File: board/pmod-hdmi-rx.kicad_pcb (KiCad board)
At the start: 2 copper layers, 42 x 43.3 mm, 59 parts, among them P1 PMOD-CONN_6X2, U31 XC9140, U32 REG710-DBV

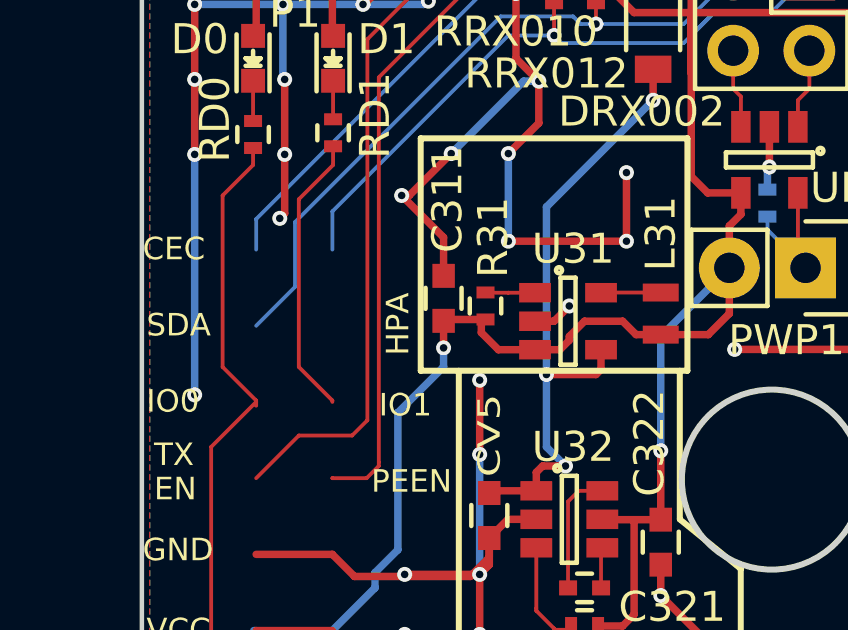
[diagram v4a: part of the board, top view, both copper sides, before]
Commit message: Update from templates + s/HPD/HOT/ + s/HPA/HOT/
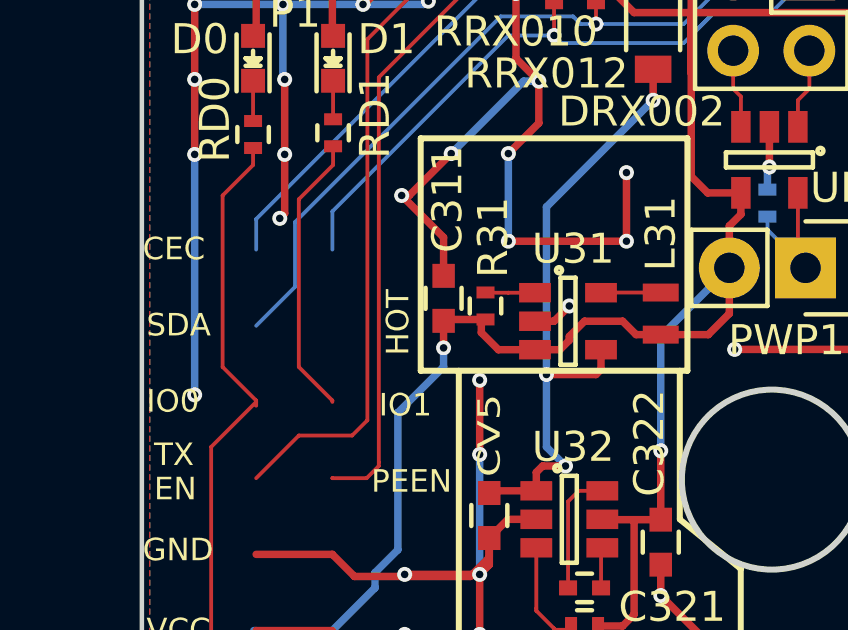
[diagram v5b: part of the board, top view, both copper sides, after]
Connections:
- net /HDMI RX/HDMIP_RX0_HPD renamed /HDMI RX/HDMIP_RX0_HOT
- P1 pad 2: /HDMI RX/HDMI_RX0_HPA -> /HDMI RX/HDMI_RX0_HOT
- QRX001 pad 1: /HDMI RX/HDMI_RX0_HPD -> /HDMI RX/HDMI_RX0_HOT
- RRX001 pad 2: /HDMI RX/HDMI_RX0_HPD -> /HDMI RX/HDMI_RX0_HOT
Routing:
- net /HDMI RX/HDMI_RX0_HPD: track 3.01 -> 0.00 mm
- net /HDMI RX/HDMI_RX0_HOT: track 0.00 -> 3.01 mm
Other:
- board text added: "HOT"
- board text removed: "HPA"
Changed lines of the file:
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@@
   (net 11 /HDMI_RX0_D2+)
   (net 12 /HDMI_RX0_D2-)
-  (net 13 "/HDMI RX/HDMIP_RX0_HPD")
+  (net 13 "/HDMI RX/HDMIP_RX0_HOT")
   (net 14 /HDMI_RX0_CEC)
   (net 15 "/HDMI RX/HDMIP_RX0_CLK+")
@@
   (net 43 /EEPROM_SCL)
   (net 44 /EEPROM_SDA)
-  (net 45 "/HDMI RX/HDMI_RX0_HPA")
+  (net 45 "/HDMI RX/HDMI_RX0_HOT")
   (net 46 /HDMI_RX0_IO1)
   (net 47 /HDMI_RX0_IO0)
@@
   (net 49 /HDMI_RX0_TXEN)
   (net 50 "Net-(PWP1-Pad1)")
-  (net 51 "/HDMI RX/HDMI_RX0_HPD")
+  (net 51 "/HDMI RX/HDMI_RX0_HOT")
   (net 52 "Net-(QRX001-Pad3)")
   (net 53 "Net-(QRX003-Pad3)")
@@
     (add_net "/HDMI RX/HDMIP_RX0_D2+")
     (add_net "/HDMI RX/HDMIP_RX0_D2-")
-    (add_net "/HDMI RX/HDMIP_RX0_HPD")
+    (add_net "/HDMI RX/HDMIP_RX0_HOT")
     (add_net "/HDMI RX/HDMIP_RX0_SCL")
     (add_net "/HDMI RX/HDMIP_RX0_SDA")
-    (add_net "/HDMI RX/HDMI_RX0_HPA")
-    (add_net "/HDMI RX/HDMI_RX0_HPD")
+    (add_net "/HDMI RX/HDMI_RX0_HOT")
+    (add_net "/HDMI RX/HDMI_RX0_HOT")
     (add_net "/HDMI RX/VCC5V0_RX0")
     (add_net "/HDMI RX/VTTI3V3")
@@
       (net 40 "Net-(FBRX004-Pad1)"))
     (pad 19 smd rect (at -4.5 -1.3 90) (size 0.3302 2.75) (layers F.Cu F.Paste F.Mask)
-      (net 13 "/HDMI RX/HDMIP_RX0_HPD"))
+      (net 13 "/HDMI RX/HDMIP_RX0_HOT"))
     (pad 0 thru_hole oval (at -7.55 0 90) (size 1.8 3.5) (drill oval 1.1 2.75) (layers *.Cu *.Mask F.SilkS))
     (pad 0 thru_hole oval (at 7.25 0 90) (size 1.8 3.5) (drill oval 1.1 2.75) (layers *.Cu *.Mask F.SilkS))
@@
     (fp_line (start -0.25 0.525) (end 0.25 0.525) (layer F.SilkS) (width 0.15))
     (pad 1 smd rect (at -0.45 0 90) (size 0.4 0.6) (layers F.Cu F.Paste F.Mask)
-      (net 13 "/HDMI RX/HDMIP_RX0_HPD"))
+      (net 13 "/HDMI RX/HDMIP_RX0_HOT"))
     (pad 2 smd rect (at 0.45 0 90) (size 0.4 0.6) (layers F.Cu F.Paste F.Mask)
       (net 38 "/HDMI RX/VCC5V0_RX0"))
@@
       (net 2 GND))
     (pad 2 smd rect (at 0.45 0 270) (size 0.4 0.6) (layers F.Cu F.Paste F.Mask)
-      (net 51 "/HDMI RX/HDMI_RX0_HPD"))
+      (net 51 "/HDMI RX/HDMI_RX0_HOT"))
     (model Resistors_SMD.3dshapes/R_0402.wrl
       (at (xyz 0 0 0))
@@
       (net 14 /HDMI_RX0_CEC))
     (pad 2 thru_hole circle (at 1.27 -3.81 270) (size 1.524 1.524) (drill 1.016) (layers *.Cu *.Mask F.SilkS)
-      (net 45 "/HDMI RX/HDMI_RX0_HPA"))
+      (net 45 "/HDMI RX/HDMI_RX0_HOT"))
     (pad 8 thru_hole circle (at -1.27 -3.81 270) (size 1.524 1.524) (drill 1.016) (layers *.Cu *.Mask F.SilkS)
       (net 28 /HDMI_RX0_SDA))
@@
     (fp_line (start 1.49982 -0.65024) (end 1.49982 0.0508) (layer F.SilkS) (width 0.15))
     (pad 1 smd rect (at -0.95 1.00076) (size 0.8001 0.8001) (layers F.Cu F.Paste F.Mask)
-      (net 51 "/HDMI RX/HDMI_RX0_HPD"))
+      (net 51 "/HDMI RX/HDMI_RX0_HOT"))
     (pad 2 smd rect (at 0.95 1.00076) (size 0.8001 0.8001) (layers F.Cu F.Paste F.Mask)
       (net 2 GND))
@@
       (net 2 GND))
     (pad 3 smd rect (at 0 -0.99822) (size 0.8001 0.8001) (layers F.Cu F.Paste F.Mask)
-      (net 13 "/HDMI RX/HDMIP_RX0_HPD"))
+      (net 13 "/HDMI RX/HDMIP_RX0_HOT"))
     (model TO_SOT_Packages_SMD.3dshapes/SOT-23.wrl
       (at (xyz 0 0 0))
@@
     (fp_line (start 1.49982 -0.65024) (end 1.49982 0.0508) (layer F.SilkS) (width 0.15))
     (pad 1 smd rect (at -0.95 1.00076) (size 0.8001 0.8001) (layers F.Cu F.Paste F.Mask)
-      (net 13 "/HDMI RX/HDMIP_RX0_HPD"))
+      (net 13 "/HDMI RX/HDMIP_RX0_HOT"))
     (pad 2 smd rect (at 0.95 1.00076) (size 0.8001 0.8001) (layers F.Cu F.Paste F.Mask)
       (net 2 GND))
@@
     (effects (font (size 1 1) (thickness 0.15)) (justify mirror))
   )
-  (gr_text HPA (at 89.662 99.314) (layer B.SilkS)
+  (gr_text HOT (at 89.662 99.314) (layer B.SilkS)
     (effects (font (size 1 1) (thickness 0.15)) (justify mirror))
   )
@@
     (effects (font (size 0.75 0.75) (thickness 0.15)) (justify left))
   )
-  (gr_text HPA (at 88.773 100.203 90) (layer F.SilkS)
+  (gr_text HOT (at 88.773 100.203 90) (layer F.SilkS)
     (effects (font (size 0.75 0.75) (thickness 0.15)) (justify left))
   )

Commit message: Temp commit.
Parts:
- moved RRX005 0.51 mm to (113.9, 83.6)
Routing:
- net /HDMI RX/HDMIP_RX0_CLK-: track 14.0 -> 12.3 mm
